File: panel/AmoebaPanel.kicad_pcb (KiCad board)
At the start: 2 copper layers, 108 x 108 mm, 228 parts, among them J1 Conn_01x01_Pin, J2 Conn_01x01_Pin, J3 Conn_01x01_Pin, J4 Conn_01x01_Pin, J5 Conn_01x01_Pin, SW1 SW_SPST

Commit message: feat(panel): label rows and thumbs on edge rails
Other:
- board text added: "Home"
- board text added: "Lower"
- board text added: "Thumb"
- board text added: "Thumb and Utility"
- board text added: "Upper"
- board text added: "Utility"
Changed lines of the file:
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@@
 		(layer "B.SilkS")
 	)
+	(gr_line
+		(start 99.85 128.5)
+		(end 96 128.5)
+		(stroke
+			(width 0.1)
+			(type default)
+		)
+		(layer "B.SilkS")
+	)
 	(gr_rect
 		(start 119.55 109.2)
@@
 	)
 	(gr_line
+		(start 202.875 128.5)
+		(end 199 128.5)
+		(stroke
+			(width 0.1)
+			(type default)
+		)
+		(layer "B.SilkS")
+	)
+	(gr_line
 		(start 170.275 114.6)
 		(end 169.425 114.6)
@@
 	)
 	(gr_line
+		(start 165.5 158.5)
+		(end 165.5 154)
+		(stroke
+			(width 0.1)
+			(type default)
+		)
+		(layer "B.SilkS")
+	)
+	(gr_line
 		(start 129.075 90.6)
 		(end 128.225 90.6)
@@
 	)
 	(gr_line
+		(start 133.5 158.5)
+		(end 133.5 154)
+		(stroke
+			(width 0.1)
+			(type default)
+		)
+		(layer "B.SilkS")
+	)
+	(gr_line
 		(start 129.775 147.075)
 		(end 129.775 147.95)
@@
 		)
 	)
+	(gr_text "Utility"
+		(at 159.55 155.85 0)
+		(layer "B.SilkS")
+		(effects
+			(font
+				(size 1 1)
+				(thickness 0.15)
+			)
+			(justify left bottom mirror)
+		)
+	)
+	(gr_text "Thumb"
+		(at 119.5 155.85 0)
+		(layer "B.SilkS")
+		(effects
+			(font
+				(size 1 1)
+				(thickness 0.15)
+			)
+			(justify left bottom mirror)
+		)
+	)
 	(gr_text "v010a1"
 		(at 144.05 96.25 0)
@@
 		)
 	)
+	(gr_text "Home"
+		(at 200.3465 93.7 -90)
+		(layer "B.SilkS")
+		(effects
+			(font
+				(size 1 1)
+				(thickness 0.15)
+			)
+			(justify left bottom mirror)
+		)
+	)
 	(gr_text "v010a1"
 		(at 112.05 120.25 0)
@@
 		)
 	)
+	(gr_text "Lower"
+		(at 200.0965 118.35 -90)
+		(layer "B.SilkS")
+		(effects
+			(font
+				(size 1 1)
+				(thickness 0.15)
+			)
+			(justify left bottom mirror)
+		)
+	)
 	(gr_text "v010a1"
 		(at 160.05 144.25 0)
@@
 		)
 	)
+	(gr_text "Lower"
+		(at 97.0465 118.2 -90)
+		(layer "B.SilkS")
+		(effects
+			(font
+				(size 1 1)
+				(thickness 0.15)
+			)
+			(justify left bottom mirror)
+		)
+	)
 	(gr_text "v010a1"
 		(at 160.05 120.25 0)
@@
 		)
 	)
+	(gr_text "Thumb and Utility"
+		(at 200.4465 147 -90)
+		(layer "B.SilkS")
+		(effects
+			(font
+				(size 1 1)
+				(thickness 0.15)
+			)
+			(justify left bottom mirror)
+		)
+	)
 	(gr_text "v010a1"
 		(at 112.05 144.25 0)
@@
 		)
 	)
+	(gr_text "Upper"
+		(at 97.3965 70.15 -90)
+		(layer "B.SilkS")
+		(effects
+			(font
+				(size 1 1)
+				(thickness 0.15)
+			)
+			(justify left bottom mirror)
+		)
+	)
+	(gr_text "Utility"
+		(at 143.3 155.85 0)
+		(layer "B.SilkS")
+		(effects
+			(font
+				(size 1 1)
+				(thickness 0.15)
+			)
+			(justify left bottom mirror)
+		)
+	)
+	(gr_text "Thumb and Utility"
+		(at 97.3965 146.85 -90)
+		(layer "B.SilkS")
+		(effects
+			(font
+				(size 1 1)
+				(thickness 0.15)
+			)
+			(justify left bottom mirror)
+		)
+	)
 	(gr_text "v010a1"
 		(at 176.05 72.25 0)
@@
 		)
 	)
+	(gr_text "Upper"
+		(at 200.4465 70.3 -90)
+		(layer "B.SilkS")
+		(effects
+			(font
+				(size 1 1)
+				(thickness 0.15)
+			)
+			(justify left bottom mirror)
+		)
+	)
 	(gr_text "v010a1"
 		(at 144.05 72.25 0)
@@
 		)
 	)
+	(gr_text "Home"
+		(at 97.2965 93.55 -90)
+		(layer "B.SilkS")
+		(effects
+			(font
+				(size 1 1)
+				(thickness 0.15)
+			)
+			(justify left bottom mirror)
+		)
+	)
 	(gr_text "v010a1"
 		(at 112.05 96.25 0)
@@
 		)
 	)
+	(gr_text "Thumb"
+		(at 183.5 155.85 0)
+		(layer "B.SilkS")
+		(effects
+			(font
+				(size 1 1)
+				(thickness 0.15)
+			)
+			(justify left bottom mirror)
+		)
+	)
 	(gr_text "Amoeba"
 		(at 106.55 143.8 0)
@@
 			(type solid)
 		)
+	)
+	(gr_text_box "This 6 x 4 panel allows much of a small Dactyl's matrix wiring to be done while still in the panel."
+		(start 153.375 51.25)
+		(end 198.425 54.8)
+		(layer "F.SilkS")
+		(effects
+			(font
+				(size 1 1)
+				(thickness 0.15)
+			)
+			(justify left top)
+		)
+		(border no)
+		(stroke
+			(width 0)
+			(type solid)
+		)

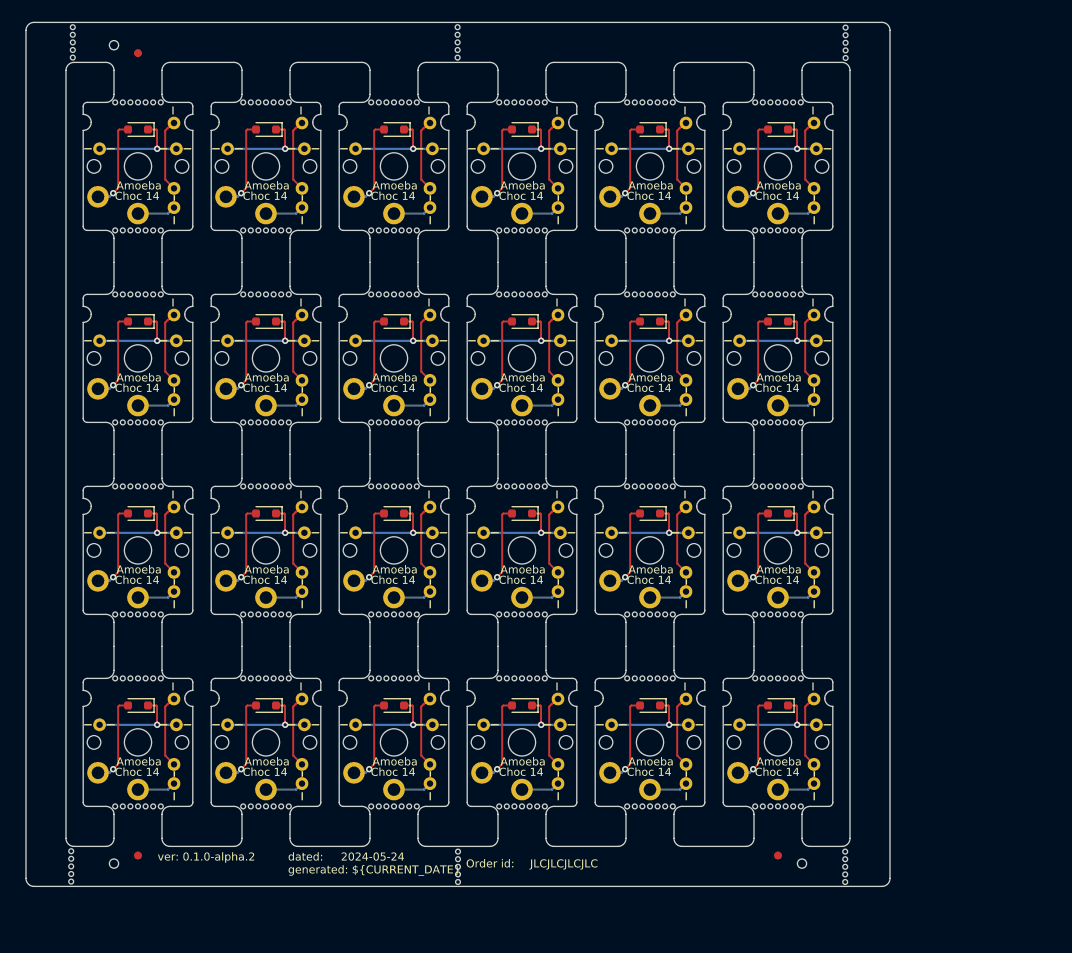
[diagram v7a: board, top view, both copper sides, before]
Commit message: feat(panel): space out to match wiring distances
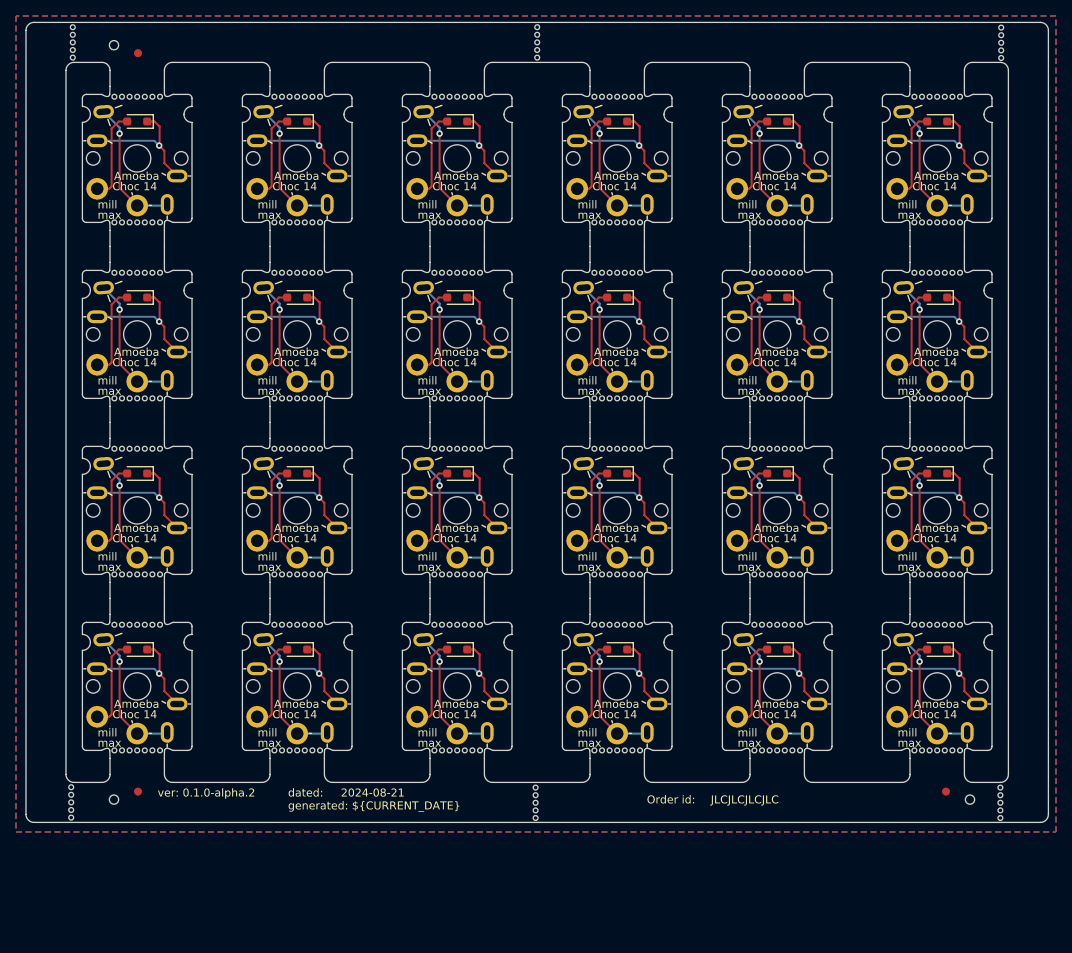
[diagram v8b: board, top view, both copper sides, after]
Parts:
- removed the D1 at (141.2, 88.2)
- removed the D1 at (109.2, 136.2)
- removed the D1 at (109.2, 64.2)
- removed the D1 at (157.2, 136.2)
- removed the D1 at (109.2, 112.2)
- removed the D1 at (141.2, 64.2)
- removed the D1 at (125.2, 64.2)
- removed the D1 at (173.2, 136.2)
- removed the D1 at (125.2, 112.2)
- removed the D1 at (173.2, 112.2)
- removed the D1 at (189.2, 112.2)
- removed the D1 at (157.2, 88.2)
- removed the D1 at (141.2, 136.2)
- removed the D1 at (189.2, 88.2)
- removed the D1 at (109.2, 88.2)
- removed the D1 at (125.2, 88.2)
- removed the D1 at (157.2, 112.2)
- removed the D1 at (125.2, 136.2)
- removed the D1 at (189.2, 136.2)
- removed the D1 at (173.2, 64.2)
- removed the D1 at (141.2, 112.2)
- removed the D1 at (173.2, 88.2)
- removed the D1 at (189.2, 64.2)
- removed the D1 at (157.2, 64.2)
- removed the J1 at (177.8, 87.4)
- removed the J1 at (177.8, 63.4)
- removed the J1 at (193.8, 135.4)
- removed the J1 at (129.8, 87.4)
- removed the J1 at (161.8, 63.4)
- removed the J1 at (145.8, 135.4)
- removed the J1 at (145.8, 111.4)
- removed the J1 at (129.8, 111.4)
- removed the J1 at (129.8, 63.4)
- removed the J1 at (113.8, 135.4)
- removed the J1 at (113.8, 63.4)
- removed the J1 at (193.8, 63.4)
- removed the J1 at (161.8, 135.4)
- removed the J1 at (177.8, 111.4)
- removed the J1 at (113.8, 111.4)
- removed the J1 at (129.8, 135.4)
- removed the J1 at (145.8, 63.4)
- removed the J1 at (193.8, 111.4)
- removed the J1 at (113.8, 87.4)
- removed the J1 at (161.8, 111.4)
- removed the J1 at (193.8, 87.4)
- removed the J1 at (177.8, 135.4)
- removed the J1 at (145.8, 87.4)
- removed the J1 at (161.8, 87.4)
- removed the J2 at (145.8, 145.9)
- removed the J2 at (145.8, 74.0)
- removed the J2 at (161.8, 74.0)
- removed the J2 at (177.8, 122.0)
- removed the J2 at (113.8, 122.0)
- removed the J2 at (193.8, 98.0)
- removed the J2 at (161.8, 145.9)
- removed the J2 at (193.8, 122.0)
- removed the J2 at (177.8, 98.0)
- removed the J2 at (113.8, 145.9)
- removed the J2 at (113.8, 98.0)
- removed the J2 at (129.8, 74.0)
- removed the J2 at (177.8, 145.9)
- removed the J2 at (161.8, 98.0)
- removed the J2 at (129.8, 145.9)
- removed the J2 at (161.8, 122.0)
- removed the J2 at (193.8, 74.0)
- removed the J2 at (129.8, 122.0)
- removed the J2 at (145.8, 122.0)
- removed the J2 at (113.8, 74.0)
- removed the J2 at (145.8, 98.0)
- removed the J2 at (177.8, 74.0)
- removed the J2 at (193.8, 145.9)
- removed the J2 at (129.8, 98.0)
- removed the J3 at (104.5, 90.6)
- removed the J3 at (136.4, 90.6)
- removed the J3 at (120.5, 138.6)
- removed the J3 at (168.4, 114.6)
- removed the J3 at (136.4, 66.6)
- removed the J3 at (184.4, 138.6)
- removed the J3 at (168.4, 66.6)
- removed the J3 at (152.4, 90.6)
- removed the J3 at (120.5, 114.6)
- removed the J3 at (136.4, 114.6)
- removed the J3 at (104.5, 66.6)
- removed the J3 at (152.4, 66.6)
- removed the J3 at (152.4, 114.6)
- removed the J3 at (184.4, 90.6)
- removed the J3 at (104.5, 114.6)
- removed the J3 at (168.4, 138.6)
- removed the J3 at (120.5, 90.6)
- removed the J3 at (104.5, 138.6)
- removed the J3 at (184.4, 66.6)
- removed the J3 at (184.4, 114.6)
- removed the J3 at (168.4, 90.6)
- removed the J3 at (136.4, 138.6)
- removed the J3 at (120.5, 66.6)
- removed the J3 at (152.4, 138.6)
- removed the J4 at (130.1, 114.6)
- removed the J4 at (194.1, 90.6)
- removed the J4 at (178.1, 138.6)
- removed the J4 at (178.1, 66.6)
- removed the J4 at (114.0, 66.6)
- removed the J4 at (130.1, 90.6)
- removed the J4 at (178.1, 114.6)
- removed the J4 at (162.1, 138.6)
- removed the J4 at (162.1, 114.6)
- removed the J4 at (146.1, 66.6)
- removed the J4 at (114.0, 138.6)
- removed the J4 at (114.0, 90.6)
- removed the J4 at (114.0, 114.6)
- removed the J4 at (162.1, 66.6)
- removed the J4 at (194.1, 114.6)
- removed the J4 at (194.1, 138.6)
- removed the J4 at (146.1, 114.6)
- removed the J4 at (130.1, 138.6)
- removed the J4 at (146.1, 90.6)
- removed the J4 at (146.1, 138.6)
- removed the J4 at (194.1, 66.6)
- removed the J4 at (178.1, 90.6)
- removed the J4 at (130.1, 66.6)
- removed the J4 at (162.1, 90.6)
- removed the J5 at (161.8, 119.5)
- removed the J5 at (193.8, 119.5)
- removed the J5 at (193.8, 71.5)
- removed the J5 at (161.8, 71.5)
- removed the J5 at (177.8, 71.5)
- removed the J5 at (129.8, 71.5)
- removed the J5 at (145.8, 119.5)
- removed the J5 at (113.8, 119.5)
- removed the J5 at (129.8, 95.5)
- removed the J5 at (113.8, 95.5)
- removed the J5 at (113.8, 71.5)
- removed the J5 at (145.8, 143.6)
- removed the J5 at (129.8, 119.5)
- removed the J5 at (129.8, 143.6)
- removed the J5 at (177.8, 143.6)
- removed the J5 at (161.8, 95.5)
- removed the J5 at (113.8, 143.6)
- removed the J5 at (177.8, 95.5)
- removed the J5 at (145.8, 71.5)
- removed the J5 at (161.8, 143.6)
- removed the J5 at (145.8, 95.5)
- removed the J5 at (177.8, 119.5)
- removed the J5 at (193.8, 143.6)
- removed the J5 at (193.8, 95.5)
- removed the REF** at (141.2, 76.8)
- removed the REF** at (157.2, 132.8)
- removed the REF** at (125.2, 148.8)
- removed the REF** at (173.2, 100.8)
- removed the REF** at (173.2, 76.8)
- removed the REF** at (125.2, 60.8)
- removed the REF** at (141.2, 60.8)
- removed the REF** at (141.2, 108.8)
- removed the REF** at (157.2, 148.8)
- removed the REF** at (109.2, 148.8)
- removed the REF** at (141.2, 132.8)
- removed the REF** at (125.2, 108.8)
- removed the REF** at (189.2, 108.8)
- removed the REF** at (189.2, 84.8)
- removed the REF** at (141.2, 84.8)
- removed the REF** at (109.2, 84.8)
- removed the REF** at (125.2, 76.8)
- removed the REF** at (189.2, 76.8)
- removed the REF** at (157.2, 108.8)
- removed the REF** at (141.2, 124.8)
- removed the REF** at (173.2, 108.8)
- removed the REF** at (157.2, 100.8)
- removed the REF** at (125.2, 124.8)
- removed the REF** at (173.2, 132.8)
- removed the REF** at (189.2, 124.8)
- removed the REF** at (125.2, 100.8)
- removed the REF** at (189.2, 132.8)
- removed the REF** at (157.2, 84.8)
- removed the REF** at (173.2, 148.8)
- removed the REF** at (157.2, 60.8)
- removed the REF** at (141.2, 100.8)
- removed the REF** at (157.2, 76.8)
- removed the REF** at (109.2, 132.8)
- removed the REF** at (189.2, 60.8)
- removed the REF** at (109.2, 108.8)
- removed the REF** at (125.2, 84.8)
- removed the REF** at (157.2, 124.8)
- removed the REF** at (173.2, 84.8)
- removed the REF** at (141.2, 148.8)
- removed the REF** at (109.2, 100.8)
- removed the REF** at (125.2, 132.8)
- removed the REF** at (173.2, 124.8)
- removed the REF** at (173.2, 60.8)
- removed the REF** at (189.2, 148.8)
- removed the REF** at (109.2, 124.8)
- removed the REF** at (109.2, 76.8)
- removed the REF** at (189.2, 100.8)
- removed the REF** at (109.2, 60.8)
- removed the SW1 at (173.2, 68.8)
- removed the SW1 at (141.2, 140.8)
- removed the SW1 at (109.2, 92.8)
- removed the SW1 at (141.2, 116.8)
- removed the SW1 at (157.2, 92.8)
- removed the SW1 at (109.2, 116.8)
- removed the SW1 at (173.2, 116.8)
- removed the SW1 at (141.2, 68.8)
- removed the SW1 at (109.2, 68.8)
- removed the SW1 at (173.2, 92.8)
- removed the SW1 at (109.2, 140.8)
- removed the SW1 at (125.2, 116.8)
- removed the SW1 at (157.2, 116.8)
- removed the SW1 at (189.2, 116.8)
- removed the SW1 at (189.2, 92.8)
- removed the SW1 at (173.2, 140.8)
- removed the SW1 at (157.2, 68.8)
- removed the SW1 at (141.2, 92.8)
- removed the SW1 at (125.2, 92.8)
- removed the SW1 at (189.2, 68.8)
- removed the SW1 at (125.2, 140.8)
- removed the SW1 at (157.2, 140.8)
- removed the SW1 at (189.2, 140.8)
- removed the SW1 at (125.2, 68.8)
- added D1: 1N4148, Diode_SMD:D_SOD-323_HandSoldering, F.Cu at (109.2, 63.2)
- added D1: 1N4148, Diode_SMD:D_SOD-323_HandSoldering, F.Cu at (129.2, 63.2)
- added D10: 1N4148, Diode_SMD:D_SOD-323_HandSoldering, F.Cu at (189.2, 85.2)
- added D11: 1N4148, Diode_SMD:D_SOD-323_HandSoldering, F.Cu at (209.2, 85.2)
- added D12: 1N4148, Diode_SMD:D_SOD-323_HandSoldering, F.Cu at (109.2, 107.2)
- added D13: 1N4148, Diode_SMD:D_SOD-323_HandSoldering, F.Cu at (129.2, 107.2)
- added D14: 1N4148, Diode_SMD:D_SOD-323_HandSoldering, F.Cu at (149.2, 107.2)
- added D15: 1N4148, Diode_SMD:D_SOD-323_HandSoldering, F.Cu at (169.2, 107.2)
- added D16: 1N4148, Diode_SMD:D_SOD-323_HandSoldering, F.Cu at (189.2, 107.2)
- added D17: 1N4148, Diode_SMD:D_SOD-323_HandSoldering, F.Cu at (209.2, 107.2)
- added D18: 1N4148, Diode_SMD:D_SOD-323_HandSoldering, F.Cu at (109.2, 129.2)
- added D19: 1N4148, Diode_SMD:D_SOD-323_HandSoldering, F.Cu at (129.2, 129.2)
- added D2: 1N4148, Diode_SMD:D_SOD-323_HandSoldering, F.Cu at (149.2, 63.2)
- added D20: 1N4148, Diode_SMD:D_SOD-323_HandSoldering, F.Cu at (149.2, 129.2)
- added D21: 1N4148, Diode_SMD:D_SOD-323_HandSoldering, F.Cu at (169.2, 129.2)
- added D22: 1N4148, Diode_SMD:D_SOD-323_HandSoldering, F.Cu at (189.2, 129.2)
- added D23: 1N4148, Diode_SMD:D_SOD-323_HandSoldering, F.Cu at (209.2, 129.2)
- added D3: 1N4148, Diode_SMD:D_SOD-323_HandSoldering, F.Cu at (169.2, 63.2)
- added D4: 1N4148, Diode_SMD:D_SOD-323_HandSoldering, F.Cu at (189.2, 63.2)
- added D5: 1N4148, Diode_SMD:D_SOD-323_HandSoldering, F.Cu at (209.2, 63.2)
- added D6: 1N4148, Diode_SMD:D_SOD-323_HandSoldering, F.Cu at (109.2, 85.2)
- added D7: 1N4148, Diode_SMD:D_SOD-323_HandSoldering, F.Cu at (129.2, 85.2)
- added D8: 1N4148, Diode_SMD:D_SOD-323_HandSoldering, F.Cu at (149.2, 85.2)
- added D9: 1N4148, Diode_SMD:D_SOD-323_HandSoldering, F.Cu at (169.2, 85.2)
- added J1: Conn_01x01_Pin, Amoeba_Choc_Nar:Pin_D0.8mm_L7.0mm, B.Cu at (105.0, 62.0)
- added J1: Conn_01x01_Pin, Amoeba_Choc_Nar:Pin_D0.8mm_L7.0mm, B.Cu at (125.0, 62.0)
- added J10: Conn_01x01_Pin, Amoeba_Choc_Nar:Pin_D0.8mm_L7.0mm, B.Cu at (172.9, 73.5)
- added J11: Conn_01x01_Pin, Amoeba_Choc_Nar:Pin_D0.8mm_L7.0mm, B.Cu at (164.2, 65.6)
- added J12: Conn_01x01_Pin, Amoeba_Choc_Nar:Pin_D0.8mm_L7.0mm, B.Cu at (174.2, 70.0)
- added J13: Conn_01x01_Pin, Amoeba_Choc_Nar:Pin_D0.8mm_L7.0mm, B.Cu at (184.9, 62.0)
- added J14: Conn_01x01_Pin, Amoeba_Choc_Nar:Pin_D0.8mm_L7.0mm, B.Cu at (192.9, 73.5)
- added J15: Conn_01x01_Pin, Amoeba_Choc_Nar:Pin_D0.8mm_L7.0mm, B.Cu at (184.2, 65.6)
- added J16: Conn_01x01_Pin, Amoeba_Choc_Nar:Pin_D0.8mm_L7.0mm, B.Cu at (194.2, 70.0)
- added J17: Conn_01x01_Pin, Amoeba_Choc_Nar:Pin_D0.8mm_L7.0mm, B.Cu at (204.9, 62.0)
- added J18: Conn_01x01_Pin, Amoeba_Choc_Nar:Pin_D0.8mm_L7.0mm, B.Cu at (212.9, 73.5)
- added J19: Conn_01x01_Pin, Amoeba_Choc_Nar:Pin_D0.8mm_L7.0mm, B.Cu at (204.2, 65.6)
- added J2: Conn_01x01_Pin, Amoeba_Choc_Nar:Pin_D0.8mm_L7.0mm, B.Cu at (132.9, 73.5)
- added J2: Conn_01x01_Pin, Amoeba_Choc_Nar:Pin_D0.8mm_L7.0mm, B.Cu at (112.9, 73.5)
- added J20: Conn_01x01_Pin, Amoeba_Choc_Nar:Pin_D0.8mm_L7.0mm, B.Cu at (214.2, 70.0)
- added J21: Conn_01x01_Pin, Amoeba_Choc_Nar:Pin_D0.8mm_L7.0mm, B.Cu at (105.0, 84.0)
- added J22: Conn_01x01_Pin, Amoeba_Choc_Nar:Pin_D0.8mm_L7.0mm, B.Cu at (125.0, 84.0)
- added J23: Conn_01x01_Pin, Amoeba_Choc_Nar:Pin_D0.8mm_L7.0mm, B.Cu at (112.9, 95.5)
- added J24: Conn_01x01_Pin, Amoeba_Choc_Nar:Pin_D0.8mm_L7.0mm, B.Cu at (132.9, 95.5)
- added J25: Conn_01x01_Pin, Amoeba_Choc_Nar:Pin_D0.8mm_L7.0mm, B.Cu at (104.2, 87.6)
- added J26: Conn_01x01_Pin, Amoeba_Choc_Nar:Pin_D0.8mm_L7.0mm, B.Cu at (124.2, 87.6)
- added J27: Conn_01x01_Pin, Amoeba_Choc_Nar:Pin_D0.8mm_L7.0mm, B.Cu at (114.2, 92.0)
- added J28: Conn_01x01_Pin, Amoeba_Choc_Nar:Pin_D0.8mm_L7.0mm, B.Cu at (134.2, 92.0)
- added J29: Conn_01x01_Pin, Amoeba_Choc_Nar:Pin_D0.8mm_L7.0mm, B.Cu at (144.9, 84.0)
- added J3: Conn_01x01_Pin, Amoeba_Choc_Nar:Pin_D0.8mm_L7.0mm, B.Cu at (124.2, 65.6)
- added J3: Conn_01x01_Pin, Amoeba_Choc_Nar:Pin_D0.8mm_L7.0mm, B.Cu at (104.2, 65.6)
- added J30: Conn_01x01_Pin, Amoeba_Choc_Nar:Pin_D0.8mm_L7.0mm, B.Cu at (152.9, 95.5)
- added J31: Conn_01x01_Pin, Amoeba_Choc_Nar:Pin_D0.8mm_L7.0mm, B.Cu at (144.2, 87.6)
- added J32: Conn_01x01_Pin, Amoeba_Choc_Nar:Pin_D0.8mm_L7.0mm, B.Cu at (154.2, 92.0)
- added J33: Conn_01x01_Pin, Amoeba_Choc_Nar:Pin_D0.8mm_L7.0mm, B.Cu at (164.9, 84.0)
- added J34: Conn_01x01_Pin, Amoeba_Choc_Nar:Pin_D0.8mm_L7.0mm, B.Cu at (172.9, 95.5)
- added J35: Conn_01x01_Pin, Amoeba_Choc_Nar:Pin_D0.8mm_L7.0mm, B.Cu at (164.2, 87.6)
- added J36: Conn_01x01_Pin, Amoeba_Choc_Nar:Pin_D0.8mm_L7.0mm, B.Cu at (174.2, 92.0)
- added J37: Conn_01x01_Pin, Amoeba_Choc_Nar:Pin_D0.8mm_L7.0mm, B.Cu at (184.9, 84.0)
- added J38: Conn_01x01_Pin, Amoeba_Choc_Nar:Pin_D0.8mm_L7.0mm, B.Cu at (192.9, 95.5)
- added J39: Conn_01x01_Pin, Amoeba_Choc_Nar:Pin_D0.8mm_L7.0mm, B.Cu at (184.2, 87.6)
- added J4: Conn_01x01_Pin, Amoeba_Choc_Nar:Pin_D0.8mm_L7.0mm, B.Cu at (114.2, 70.0)
- added J4: Conn_01x01_Pin, Amoeba_Choc_Nar:Pin_D0.8mm_L7.0mm, B.Cu at (134.2, 70.0)
- added J40: Conn_01x01_Pin, Amoeba_Choc_Nar:Pin_D0.8mm_L7.0mm, B.Cu at (194.2, 92.0)
- added J41: Conn_01x01_Pin, Amoeba_Choc_Nar:Pin_D0.8mm_L7.0mm, B.Cu at (204.9, 84.0)
- added J42: Conn_01x01_Pin, Amoeba_Choc_Nar:Pin_D0.8mm_L7.0mm, B.Cu at (212.9, 95.5)
- added J43: Conn_01x01_Pin, Amoeba_Choc_Nar:Pin_D0.8mm_L7.0mm, B.Cu at (204.2, 87.6)
- added J44: Conn_01x01_Pin, Amoeba_Choc_Nar:Pin_D0.8mm_L7.0mm, B.Cu at (214.2, 92.0)
- added J45: Conn_01x01_Pin, Amoeba_Choc_Nar:Pin_D0.8mm_L7.0mm, B.Cu at (105.0, 106.0)
- added J46: Conn_01x01_Pin, Amoeba_Choc_Nar:Pin_D0.8mm_L7.0mm, B.Cu at (125.0, 106.0)
- added J47: Conn_01x01_Pin, Amoeba_Choc_Nar:Pin_D0.8mm_L7.0mm, B.Cu at (112.9, 117.5)
- added J48: Conn_01x01_Pin, Amoeba_Choc_Nar:Pin_D0.8mm_L7.0mm, B.Cu at (132.9, 117.5)
- added J49: Conn_01x01_Pin, Amoeba_Choc_Nar:Pin_D0.8mm_L7.0mm, B.Cu at (104.2, 109.6)
- added J5: Conn_01x01_Pin, Amoeba_Choc_Nar:Pin_D0.8mm_L7.0mm, B.Cu at (144.9, 62.0)
- added J50: Conn_01x01_Pin, Amoeba_Choc_Nar:Pin_D0.8mm_L7.0mm, B.Cu at (124.2, 109.6)
- added J51: Conn_01x01_Pin, Amoeba_Choc_Nar:Pin_D0.8mm_L7.0mm, B.Cu at (114.2, 114.0)
- added J52: Conn_01x01_Pin, Amoeba_Choc_Nar:Pin_D0.8mm_L7.0mm, B.Cu at (134.2, 114.0)
- added J53: Conn_01x01_Pin, Amoeba_Choc_Nar:Pin_D0.8mm_L7.0mm, B.Cu at (144.9, 106.0)
- added J54: Conn_01x01_Pin, Amoeba_Choc_Nar:Pin_D0.8mm_L7.0mm, B.Cu at (152.9, 117.5)
- added J55: Conn_01x01_Pin, Amoeba_Choc_Nar:Pin_D0.8mm_L7.0mm, B.Cu at (144.2, 109.6)
- added J56: Conn_01x01_Pin, Amoeba_Choc_Nar:Pin_D0.8mm_L7.0mm, B.Cu at (154.2, 114.0)
- added J57: Conn_01x01_Pin, Amoeba_Choc_Nar:Pin_D0.8mm_L7.0mm, B.Cu at (164.9, 106.0)
- added J58: Conn_01x01_Pin, Amoeba_Choc_Nar:Pin_D0.8mm_L7.0mm, B.Cu at (172.9, 117.5)
- added J59: Conn_01x01_Pin, Amoeba_Choc_Nar:Pin_D0.8mm_L7.0mm, B.Cu at (164.2, 109.6)
- added J6: Conn_01x01_Pin, Amoeba_Choc_Nar:Pin_D0.8mm_L7.0mm, B.Cu at (152.9, 73.5)
- added J60: Conn_01x01_Pin, Amoeba_Choc_Nar:Pin_D0.8mm_L7.0mm, B.Cu at (174.2, 114.0)
- added J61: Conn_01x01_Pin, Amoeba_Choc_Nar:Pin_D0.8mm_L7.0mm, B.Cu at (184.9, 106.0)
- added J62: Conn_01x01_Pin, Amoeba_Choc_Nar:Pin_D0.8mm_L7.0mm, B.Cu at (192.9, 117.5)
- added J63: Conn_01x01_Pin, Amoeba_Choc_Nar:Pin_D0.8mm_L7.0mm, B.Cu at (184.2, 109.6)
- added J64: Conn_01x01_Pin, Amoeba_Choc_Nar:Pin_D0.8mm_L7.0mm, B.Cu at (194.2, 114.0)
- added J65: Conn_01x01_Pin, Amoeba_Choc_Nar:Pin_D0.8mm_L7.0mm, B.Cu at (204.9, 106.0)
- added J66: Conn_01x01_Pin, Amoeba_Choc_Nar:Pin_D0.8mm_L7.0mm, B.Cu at (212.9, 117.5)
- added J67: Conn_01x01_Pin, Amoeba_Choc_Nar:Pin_D0.8mm_L7.0mm, B.Cu at (204.2, 109.6)
- added J68: Conn_01x01_Pin, Amoeba_Choc_Nar:Pin_D0.8mm_L7.0mm, B.Cu at (214.2, 114.0)
- added J69: Conn_01x01_Pin, Amoeba_Choc_Nar:Pin_D0.8mm_L7.0mm, B.Cu at (105.0, 128.0)
- added J7: Conn_01x01_Pin, Amoeba_Choc_Nar:Pin_D0.8mm_L7.0mm, B.Cu at (144.2, 65.6)
- added J70: Conn_01x01_Pin, Amoeba_Choc_Nar:Pin_D0.8mm_L7.0mm, B.Cu at (125.0, 128.0)
- added J71: Conn_01x01_Pin, Amoeba_Choc_Nar:Pin_D0.8mm_L7.0mm, B.Cu at (112.9, 139.6)
- added J72: Conn_01x01_Pin, Amoeba_Choc_Nar:Pin_D0.8mm_L7.0mm, B.Cu at (132.9, 139.6)
- added J73: Conn_01x01_Pin, Amoeba_Choc_Nar:Pin_D0.8mm_L7.0mm, B.Cu at (104.2, 131.6)
- added J74: Conn_01x01_Pin, Amoeba_Choc_Nar:Pin_D0.8mm_L7.0mm, B.Cu at (124.2, 131.6)
- added J75: Conn_01x01_Pin, Amoeba_Choc_Nar:Pin_D0.8mm_L7.0mm, B.Cu at (114.2, 136.0)
- added J76: Conn_01x01_Pin, Amoeba_Choc_Nar:Pin_D0.8mm_L7.0mm, B.Cu at (134.2, 136.0)
- added J77: Conn_01x01_Pin, Amoeba_Choc_Nar:Pin_D0.8mm_L7.0mm, B.Cu at (144.9, 128.0)
- added J78: Conn_01x01_Pin, Amoeba_Choc_Nar:Pin_D0.8mm_L7.0mm, B.Cu at (152.9, 139.6)
- added J79: Conn_01x01_Pin, Amoeba_Choc_Nar:Pin_D0.8mm_L7.0mm, B.Cu at (144.2, 131.6)
- added J8: Conn_01x01_Pin, Amoeba_Choc_Nar:Pin_D0.8mm_L7.0mm, B.Cu at (154.2, 70.0)
- added J80: Conn_01x01_Pin, Amoeba_Choc_Nar:Pin_D0.8mm_L7.0mm, B.Cu at (154.2, 136.0)
- added J81: Conn_01x01_Pin, Amoeba_Choc_Nar:Pin_D0.8mm_L7.0mm, B.Cu at (164.9, 128.0)
- added J82: Conn_01x01_Pin, Amoeba_Choc_Nar:Pin_D0.8mm_L7.0mm, B.Cu at (172.9, 139.6)
- added J83: Conn_01x01_Pin, Amoeba_Choc_Nar:Pin_D0.8mm_L7.0mm, B.Cu at (164.2, 131.6)
- added J84: Conn_01x01_Pin, Amoeba_Choc_Nar:Pin_D0.8mm_L7.0mm, B.Cu at (174.2, 136.0)
- added J85: Conn_01x01_Pin, Amoeba_Choc_Nar:Pin_D0.8mm_L7.0mm, B.Cu at (184.9, 128.0)
- added J86: Conn_01x01_Pin, Amoeba_Choc_Nar:Pin_D0.8mm_L7.0mm, B.Cu at (192.9, 139.6)
- added J87: Conn_01x01_Pin, Amoeba_Choc_Nar:Pin_D0.8mm_L7.0mm, B.Cu at (184.2, 131.6)
- added J88: Conn_01x01_Pin, Amoeba_Choc_Nar:Pin_D0.8mm_L7.0mm, B.Cu at (194.2, 136.0)
- added J89: Conn_01x01_Pin, Amoeba_Choc_Nar:Pin_D0.8mm_L7.0mm, B.Cu at (204.9, 128.0)
- added J9: Conn_01x01_Pin, Amoeba_Choc_Nar:Pin_D0.8mm_L7.0mm, B.Cu at (164.9, 62.0)
- added J90: Conn_01x01_Pin, Amoeba_Choc_Nar:Pin_D0.8mm_L7.0mm, B.Cu at (212.9, 139.6)
- added J91: Conn_01x01_Pin, Amoeba_Choc_Nar:Pin_D0.8mm_L7.0mm, B.Cu at (204.2, 131.6)
- added J92: Conn_01x01_Pin, Amoeba_Choc_Nar:Pin_D0.8mm_L7.0mm, B.Cu at (214.2, 136.0)
- added REF**: Mouse_Bites, Amoeba_Choc_Nar:Mouse_Bites, F.Cu at (109.2, 75.8)
- added REF**: Mouse_Bites, Amoeba_Choc_Nar:Mouse_Bites, F.Cu at (109.2, 60.1)
- added REF**: Mouse_Bites, Amoeba_Choc_Nar:Mouse_Bites, F.Cu at (129.2, 75.8)
- added REF**: Mouse_Bites, Amoeba_Choc_Nar:Mouse_Bites, F.Cu at (129.2, 60.1)
- added REF**1: Mouse_Bites, Amoeba_Choc_Nar:Mouse_Bites, F.Cu at (149.2, 75.8)
- added REF**10: Mouse_Bites, Amoeba_Choc_Nar:Mouse_Bites, F.Cu at (129.2, 97.8)
- added REF**11: Mouse_Bites, Amoeba_Choc_Nar:Mouse_Bites, F.Cu at (109.2, 82.1)
- added REF**12: Mouse_Bites, Amoeba_Choc_Nar:Mouse_Bites, F.Cu at (129.2, 82.1)
- added REF**13: Mouse_Bites, Amoeba_Choc_Nar:Mouse_Bites, F.Cu at (149.2, 97.8)
- added REF**14: Mouse_Bites, Amoeba_Choc_Nar:Mouse_Bites, F.Cu at (149.2, 82.1)
- added REF**15: Mouse_Bites, Amoeba_Choc_Nar:Mouse_Bites, F.Cu at (169.2, 97.8)
- added REF**16: Mouse_Bites, Amoeba_Choc_Nar:Mouse_Bites, F.Cu at (169.2, 82.1)
- added REF**17: Mouse_Bites, Amoeba_Choc_Nar:Mouse_Bites, F.Cu at (189.2, 97.8)
- added REF**18: Mouse_Bites, Amoeba_Choc_Nar:Mouse_Bites, F.Cu at (189.2, 82.1)
- added REF**19: Mouse_Bites, Amoeba_Choc_Nar:Mouse_Bites, F.Cu at (209.2, 97.8)
- added REF**2: Mouse_Bites, Amoeba_Choc_Nar:Mouse_Bites, F.Cu at (149.2, 60.1)
- added REF**20: Mouse_Bites, Amoeba_Choc_Nar:Mouse_Bites, F.Cu at (209.2, 82.1)
- added REF**21: Mouse_Bites, Amoeba_Choc_Nar:Mouse_Bites, F.Cu at (109.2, 119.8)
- added REF**22: Mouse_Bites, Amoeba_Choc_Nar:Mouse_Bites, F.Cu at (129.2, 119.8)
- added REF**23: Mouse_Bites, Amoeba_Choc_Nar:Mouse_Bites, F.Cu at (109.2, 104.1)
- added REF**24: Mouse_Bites, Amoeba_Choc_Nar:Mouse_Bites, F.Cu at (129.2, 104.1)
- added REF**25: Mouse_Bites, Amoeba_Choc_Nar:Mouse_Bites, F.Cu at (149.2, 119.8)
- added REF**26: Mouse_Bites, Amoeba_Choc_Nar:Mouse_Bites, F.Cu at (149.2, 104.1)
- added REF**27: Mouse_Bites, Amoeba_Choc_Nar:Mouse_Bites, F.Cu at (169.2, 119.8)
- added REF**28: Mouse_Bites, Amoeba_Choc_Nar:Mouse_Bites, F.Cu at (169.2, 104.1)
- added REF**29: Mouse_Bites, Amoeba_Choc_Nar:Mouse_Bites, F.Cu at (189.2, 119.8)
- added REF**3: Mouse_Bites, Amoeba_Choc_Nar:Mouse_Bites, F.Cu at (169.2, 75.8)
- added REF**30: Mouse_Bites, Amoeba_Choc_Nar:Mouse_Bites, F.Cu at (189.2, 104.1)
- added REF**31: Mouse_Bites, Amoeba_Choc_Nar:Mouse_Bites, F.Cu at (209.2, 119.8)
- added REF**32: Mouse_Bites, Amoeba_Choc_Nar:Mouse_Bites, F.Cu at (209.2, 104.1)
- added REF**33: Mouse_Bites, Amoeba_Choc_Nar:Mouse_Bites, F.Cu at (109.2, 141.8)
- added REF**34: Mouse_Bites, Amoeba_Choc_Nar:Mouse_Bites, F.Cu at (129.2, 141.8)
- added REF**35: Mouse_Bites, Amoeba_Choc_Nar:Mouse_Bites, F.Cu at (109.2, 126.1)
- added REF**36: Mouse_Bites, Amoeba_Choc_Nar:Mouse_Bites, F.Cu at (129.2, 126.1)
- added REF**37: Mouse_Bites, Amoeba_Choc_Nar:Mouse_Bites, F.Cu at (149.2, 141.8)
- added REF**38: Mouse_Bites, Amoeba_Choc_Nar:Mouse_Bites, F.Cu at (149.2, 126.1)
- added REF**39: Mouse_Bites, Amoeba_Choc_Nar:Mouse_Bites, F.Cu at (169.2, 141.8)
- added REF**4: Mouse_Bites, Amoeba_Choc_Nar:Mouse_Bites, F.Cu at (169.2, 60.1)
- added REF**40: Mouse_Bites, Amoeba_Choc_Nar:Mouse_Bites, F.Cu at (169.2, 126.1)
- added REF**41: Mouse_Bites, Amoeba_Choc_Nar:Mouse_Bites, F.Cu at (189.2, 141.8)
- added REF**42: Mouse_Bites, Amoeba_Choc_Nar:Mouse_Bites, F.Cu at (189.2, 126.1)
- added REF**43: Mouse_Bites, Amoeba_Choc_Nar:Mouse_Bites, F.Cu at (209.2, 141.8)
- added REF**44: Mouse_Bites, Amoeba_Choc_Nar:Mouse_Bites, F.Cu at (209.2, 126.1)
- added REF**5: Mouse_Bites, Amoeba_Choc_Nar:Mouse_Bites, F.Cu at (189.2, 75.8)
- added REF**6: Mouse_Bites, Amoeba_Choc_Nar:Mouse_Bites, F.Cu at (189.2, 60.1)
- added REF**7: Mouse_Bites, Amoeba_Choc_Nar:Mouse_Bites, F.Cu at (209.2, 75.8)
- added REF**8: Mouse_Bites, Amoeba_Choc_Nar:Mouse_Bites, F.Cu at (209.2, 60.1)
- added REF**9: Mouse_Bites, Amoeba_Choc_Nar:Mouse_Bites, F.Cu at (109.2, 97.8)
- added SW1: SW_SPST, Amoeba_Choc_Nar:pg1350-hotswap, F.Cu at (109.2, 67.8)
- added SW1: SW_SPST, Amoeba_Choc_Nar:pg1350-hotswap, F.Cu at (129.2, 67.8)
- added SW10: SW_SPST, Amoeba_Choc_Nar:pg1350-hotswap, F.Cu at (189.2, 89.8)
- added SW11: SW_SPST, Amoeba_Choc_Nar:pg1350-hotswap, F.Cu at (209.2, 89.8)
- added SW12: SW_SPST, Amoeba_Choc_Nar:pg1350-hotswap, F.Cu at (109.2, 111.8)
- added SW13: SW_SPST, Amoeba_Choc_Nar:pg1350-hotswap, F.Cu at (129.2, 111.8)
- added SW14: SW_SPST, Amoeba_Choc_Nar:pg1350-hotswap, F.Cu at (149.2, 111.8)
- added SW15: SW_SPST, Amoeba_Choc_Nar:pg1350-hotswap, F.Cu at (169.2, 111.8)
- added SW16: SW_SPST, Amoeba_Choc_Nar:pg1350-hotswap, F.Cu at (189.2, 111.8)
- added SW17: SW_SPST, Amoeba_Choc_Nar:pg1350-hotswap, F.Cu at (209.2, 111.8)
- added SW18: SW_SPST, Amoeba_Choc_Nar:pg1350-hotswap, F.Cu at (109.2, 133.8)
- added SW19: SW_SPST, Amoeba_Choc_Nar:pg1350-hotswap, F.Cu at (129.2, 133.8)
- added SW2: SW_SPST, Amoeba_Choc_Nar:pg1350-hotswap, F.Cu at (149.2, 67.8)
- added SW20: SW_SPST, Amoeba_Choc_Nar:pg1350-hotswap, F.Cu at (149.2, 133.8)
- added SW21: SW_SPST, Amoeba_Choc_Nar:pg1350-hotswap, F.Cu at (169.2, 133.8)
- added SW22: SW_SPST, Amoeba_Choc_Nar:pg1350-hotswap, F.Cu at (189.2, 133.8)
- added SW23: SW_SPST, Amoeba_Choc_Nar:pg1350-hotswap, F.Cu at (209.2, 133.8)
- added SW3: SW_SPST, Amoeba_Choc_Nar:pg1350-hotswap, F.Cu at (169.2, 67.8)
- added SW4: SW_SPST, Amoeba_Choc_Nar:pg1350-hotswap, F.Cu at (189.2, 67.8)
- added SW5: SW_SPST, Amoeba_Choc_Nar:pg1350-hotswap, F.Cu at (209.2, 67.8)
- added SW6: SW_SPST, Amoeba_Choc_Nar:pg1350-hotswap, F.Cu at (109.2, 89.8)
- added SW7: SW_SPST, Amoeba_Choc_Nar:pg1350-hotswap, F.Cu at (129.2, 89.8)
- added SW8: SW_SPST, Amoeba_Choc_Nar:pg1350-hotswap, F.Cu at (149.2, 89.8)
- added SW9: SW_SPST, Amoeba_Choc_Nar:pg1350-hotswap, F.Cu at (169.2, 89.8)
- moved ? 22.5 mm to (213.2, 147.9)
- moved REF** 22.5 mm to (210.2, 146.9)
- moved REF** 21.0 mm to (217.1, 148.3)
- moved REF** 19.5 mm to (217.2, 53.4)
- moved REF** 12.6 mm to (158.9, 148.3)
- moved REF** 9.95 mm to (159.2, 53.3)
- moved ? 8.00 mm to (106.2, 147.9)
- moved REF** 8.00 mm to (109.2, 146.9)
- moved REF** 8.00 mm to (100.9, 148.3)
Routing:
- net /row: track 314.3 -> 401.9 mm
- net /col: track 390.5 -> 415.0 mm, vias 0 -> 24
- net Net-(D1-A): track 274.5 -> 275.2 mm, vias 24 -> 0
- added copper zone on B.Cu, net (none)
- added copper zone on F.Cu, net (none)
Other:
- board size 108 x 108 mm -> 127.8 x 100 mm
- board text added: "v010a2"
- board text removed: "v010a1"
